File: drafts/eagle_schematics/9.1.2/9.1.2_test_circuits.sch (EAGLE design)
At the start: 1 part

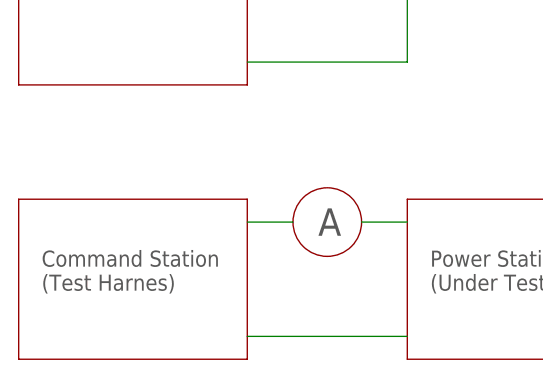
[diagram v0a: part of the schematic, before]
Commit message: Fixed misspelling of "Harness".
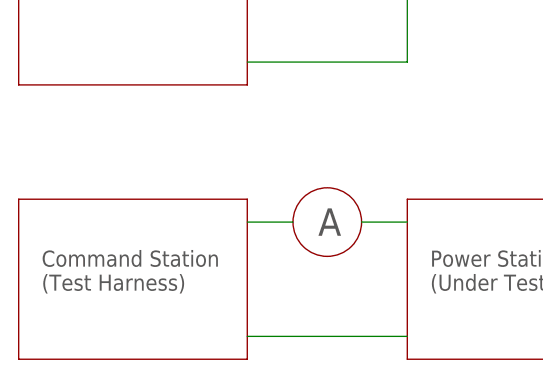
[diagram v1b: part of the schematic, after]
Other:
- note added: "Command Station (Test Harness)"
- note removed: "Command Station (Test Harnes)"
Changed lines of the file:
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@@
 <?xml version="1.0" encoding="utf-8"?>
 <!DOCTYPE eagle SYSTEM "eagle.dtd">
-<eagle version="9.6.0">
+<eagle version="9.6.2">
 <drawing>
 <settings>
-<setting alwaysvectorfont="yes"/>
+<setting alwaysvectorfont="no"/>
 <setting verticaltext="up"/>
 </settings>
@@
 <wire x1="53.34" y1="96.52" x2="53.34" y2="78.74" width="0.1524" layer="94"/>
 <text x="30.48" y="86.36" size="1.778" layer="97">Command Station
-(Test Harnes)</text>
+(Test Harness)</text>
 <wire x1="71.12" y1="96.52" x2="71.12" y2="78.74" width="0.1524" layer="94"/>
 <wire x1="71.12" y1="96.52" x2="96.52" y2="96.52" width="0.1524" layer="94"/>
